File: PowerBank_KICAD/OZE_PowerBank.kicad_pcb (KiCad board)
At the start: 2 copper layers, 0 parts

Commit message: PCB layout
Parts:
- added 100k1: R, Resistor_SMD:R_0603_1608Metric_Pad0.98x0.95mm_HandSolder, F.Cu at (222.9, 121.0)
- added C1: 100nF, Capacitor_SMD:C_0805_2012Metric_Pad1.18x1.45mm_HandSolder, F.Cu at (129.5, 121.5)
- added C10: 22uF, Capacitor_SMD:C_0805_2012Metric_Pad1.18x1.45mm_HandSolder, F.Cu at (162.0, 84.0)
- added C11: 100n, Capacitor_SMD:C_0402_1005Metric, F.Cu at (186.6, 108.3)
- added C12: 10u, Capacitor_SMD:C_0805_2012Metric_Pad1.18x1.45mm_HandSolder, F.Cu at (176.5, 107.0)
- added C13: 100n, Capacitor_SMD:C_0402_1005Metric, F.Cu at (134.0, 83.0)
- added C14: 1u, Capacitor_SMD:C_0805_2012Metric_Pad1.18x1.45mm_HandSolder, F.Cu at (176.6, 109.5)
- added C15: 100n, Capacitor_SMD:C_0402_1005Metric, F.Cu at (178.6, 103.8)
- added C16: 1u, Capacitor_SMD:C_0805_2012Metric_Pad1.18x1.45mm_HandSolder, F.Cu at (176.6, 113.5)
- added C17: 1uF, Capacitor_SMD:C_0805_2012Metric_Pad1.18x1.45mm_HandSolder, F.Cu at (126.5, 54.0)
- added C18: 22uF, Capacitor_SMD:C_0805_2012Metric_Pad1.18x1.45mm_HandSolder, F.Cu at (126.5, 50.0)
- added C19: 1uF, Capacitor_SMD:C_0805_2012Metric_Pad1.18x1.45mm_HandSolder, F.Cu at (156.1, 57.0)
- added C2: 100nF, Capacitor_SMD:C_0805_2012Metric_Pad1.18x1.45mm_HandSolder, F.Cu at (130.7, 104.3)
- added C20: 1uF, Capacitor_SMD:C_0805_2012Metric_Pad1.18x1.45mm_HandSolder, F.Cu at (154.6, 61.5)
- added C21: 865060657011, 865060657011:CAPAE1030X1050N, F.Cu at (137.5, 48.8)
- added C22: 47uF, Capacitor_SMD:C_0805_2012Metric_Pad1.18x1.45mm_HandSolder, F.Cu at (213.2, 115.8)
- added C23: 47uF, Capacitor_SMD:C_0805_2012Metric_Pad1.18x1.45mm_HandSolder, F.Cu at (216.9, 116.0)
- added C24: 47uF, Capacitor_SMD:C_0805_2012Metric_Pad1.18x1.45mm_HandSolder, F.Cu at (209.7, 115.8)
- added C25: 10u, Capacitor_SMD:C_0805_2012Metric_Pad1.18x1.45mm_HandSolder, F.Cu at (210.1, 111.3)
- added C26: 0,1uF, Capacitor_SMD:C_0805_2012Metric_Pad1.18x1.45mm_HandSolder, F.Cu at (206.2, 115.8)
- added C27: 100n, Capacitor_SMD:C_0402_1005Metric, F.Cu at (214.1, 111.3)
- added C28: 865060657011, 865060657011:CAPAE1030X1050N, F.Cu at (196.4, 49.0)
- added C29: 22uF, Capacitor_SMD:C_0805_2012Metric_Pad1.18x1.45mm_HandSolder, F.Cu at (204.6, 44.5)
- added C3: 10p, Capacitor_SMD:C_0402_1005Metric, F.Cu at (176.5, 103.5)
- added C30: 100n, Capacitor_SMD:C_0402_1005Metric, F.Cu at (157.6, 66.0)
- added C31: 10uF, Capacitor_SMD:C_0805_2012Metric_Pad1.18x1.45mm_HandSolder, F.Cu at (220.6, 103.8)
- added C32: 10uF, Capacitor_SMD:C_0805_2012Metric_Pad1.18x1.45mm_HandSolder, F.Cu at (228.7, 114.8)
- added C33: 0,1uF, Capacitor_SMD:C_0805_2012Metric_Pad1.18x1.45mm_HandSolder, F.Cu at (205.1, 98.8)
- added C34: 22u, Capacitor_SMD:C_0805_2012Metric_Pad1.18x1.45mm_HandSolder, F.Cu at (166.0, 35.5)
- added C35: 22u, Capacitor_SMD:C_0805_2012Metric_Pad1.18x1.45mm_HandSolder, F.Cu at (216.3, 123.1)
- added C4: 4.7uF, Capacitor_SMD:C_0805_2012Metric_Pad1.18x1.45mm_HandSolder, F.Cu at (153.5, 84.4)
- added C5: 10u, Capacitor_SMD:C_0805_2012Metric_Pad1.18x1.45mm_HandSolder, F.Cu at (173.5, 84.5)
- added C6: 10p, Capacitor_SMD:C_0402_1005Metric, F.Cu at (176.5, 101.0)
- added C7: 100n, Capacitor_SMD:C_0402_1005Metric, F.Cu at (181.6, 95.8)
- added C8: 100n, Capacitor_SMD:C_0402_1005Metric, F.Cu at (191.6, 99.8)
- added C9: 100n, Capacitor_SMD:C_0402_1005Metric, F.Cu at (178.5, 99.7)
- added D1: BLUE, LED_SMD:LED_1206_3216Metric_Pad1.42x1.75mm_HandSolder, F.Cu at (195.6, 121.3)
- added D10: SMAJ5.0CA, Diode_SMD:D_SMA, F.Cu at (218.6, 97.8)
- added D2: RED, LED_SMD:LED_1206_3216Metric_Pad1.42x1.75mm_HandSolder, F.Cu at (167.5, 84.5)
- added D3: SD24_SOD323, Diode_SMD:D_SOD-323, F.Cu at (143.3, 74.7)
- added D4: SZMM3Z10VST1G, Diode_SMD:D_SOD-323, F.Cu at (143.4, 65.2)
- added D5: SS14, Diode_SMD:D_SMA, F.Cu at (177.6, 62.5)
- added D6: SS14, Diode_SMD:D_SMA, F.Cu at (152.1, 51.5)
- added D7: SS14, Diode_SMD:D_SMA, F.Cu at (165.6, 51.5)
- added D8: BLUE, LED_SMD:LED_1206_3216Metric_Pad1.42x1.75mm_HandSolder, F.Cu at (188.1, 66.0)
- added D9: SMAJ5.0CA, Diode_SMD:D_SMA, F.Cu at (213.6, 95.8)
- added F1: Polyfuse, Fuse:Fuse_2920_7451Metric_Pad2.10x5.45mm_HandSolder, F.Cu at (142.4, 83.0)
- added FB1: 120R, Resistor_SMD:R_0603_1608Metric_Pad0.98x0.95mm_HandSolder, F.Cu at (176.6, 111.5)
- added H1: MountingHole, MountingHole:MountingHole_2.2mm_M2_ISO7380, F.Cu at (233.5, 137.5)
- added H2: MountingHole, MountingHole:MountingHole_2.2mm_M2_ISO7380, F.Cu at (233.5, 33.0)
- added H3: MountingHole, MountingHole:MountingHole_2.2mm_M2_ISO7380, F.Cu at (123.0, 139.5)
- added H4: MountingHole, MountingHole:MountingHole_2.2mm_M2_ISO7380, F.Cu at (124.0, 31.5)
- added IC1: TPS25810RVCR, TPS25810RVCR:QFN50P300X400X80-21N, F.Cu at (222.4, 116.8)
- added IC2: TPS2514ADBVT, TPS2514ADBVT:SOT95P280X145-6N, F.Cu at (208.8, 98.8)
- added J1: Conn_01x02_Pin, TerminalBlock_Phoenix:TerminalBlock_Phoenix_PT-1,5-2-5.0-H_1x02_P5.00mm_Horizontal, F.Cu at (126.5, 79.5)
- added J10: USB_A, Connector_USB:USB_A_TE_292303-7_Horizontal, F.Cu at (230.6, 99.3)
- added J11: Conn_01x04_Pin, TerminalBlock_Phoenix:TerminalBlock_Phoenix_PT-1,5-4-3.5-H_1x04_P3.50mm_Horizontal, F.Cu at (159.2, 34.3)
- added J12: Conn_01x04_Pin, TerminalBlock_Phoenix:TerminalBlock_Phoenix_PT-1,5-4-5.0-H_1x04_P5.00mm_Horizontal, F.Cu at (209.0, 135.5)
- added J13: Conn_01x04_Pin, Connector_PinSocket_2.54mm:PinSocket_1x04_P2.54mm_Vertical, F.Cu at (169.2, 79.4)
- added J14: Conn_01x04_Pin, Connector_PinSocket_2.54mm:PinSocket_1x04_P2.54mm_Vertical, F.Cu at (217.7, 127.5)
- added J15: Conn_01x04_Pin, Connector_PinSocket_2.54mm:PinSocket_1x04_P2.54mm_Vertical, F.Cu at (180.1, 35.5)
- added J16: Conn_01x02_Pin, Connector_JST:JST_XH_B2B-XH-A_1x02_P2.50mm_Vertical, F.Cu at (229.0, 44.0)
- added J17: Battery with BMS Input, TerminalBlock_Phoenix:TerminalBlock_Phoenix_PT-1,5-2-5.0-H_1x02_P5.00mm_Horizontal, F.Cu at (226.9, 61.0)
- added J2: DCJ200-10-A-XX-K_REVA, Connector_BarrelJack:BarrelJack_GCT_DCJ200-10-A_Horizontal, F.Cu at (130.3, 67.5)
- added J3: Conn_01x04_Pin, Connector_PinSocket_2.54mm:PinSocket_1x04_P2.54mm_Vertical, F.Cu at (194.6, 79.3)
- added J4: Conn_01x04_Pin, Connector_PinSocket_2.54mm:PinSocket_1x04_P2.54mm_Vertical, F.Cu at (182.8, 121.2)
- added J5: Conn_01x04_Pin, Connector_PinSocket_2.54mm:PinSocket_1x04_P2.54mm_Vertical, F.Cu at (187.6, 79.3)
- added J6: Conn_01x04_Pin, Connector_PinSocket_2.54mm:PinSocket_1x04_P2.54mm_Vertical, F.Cu at (201.1, 79.3)
- added J7: Conn_01x10_Pin, Connector_PinSocket_2.54mm:PinSocket_1x10_P2.54mm_Vertical, F.Cu at (211.1, 65.1)
- added J8: Conn_01x10_Pin, Connector_PinSocket_2.54mm:PinSocket_1x10_P2.54mm_Vertical, F.Cu at (158.5, 105.5)
- added J9: USB_C_Receptacle_PowerOnly_6P, Connector_USB:USB_C_Receptacle_GCT_USB4125-xx-x-0190_6P_TopMnt_Horizontal, F.Cu at (234.7, 117.8)
- added L1: 150uH, Inductor_SMD:L_Pulse_PA4320, F.Cu at (181.1, 48.5)
- added Q1: IRLML6402TRPBF, IRLML6402TRPBF:SOT95P237X112-3N, F.Cu at (143.4, 70.1)
- added Q2: IRLZ44N, Package_TO_SOT_THT:TO-220-3_Vertical, F.Cu at (148.0, 45.5)
- added Q3: IRLZ44N, Package_TO_SOT_THT:TO-220-3_Vertical, F.Cu at (161.6, 45.5)
- added R1: 10k, Resistor_SMD:R_0805_2012Metric_Pad1.20x1.40mm_HandSolder, F.Cu at (126.5, 121.5)
- added R10: 0, Resistor_SMD:R_0805_2012Metric_Pad1.20x1.40mm_HandSolder, F.Cu at (164.0, 115.6)
- added R11: 0, Resistor_SMD:R_0805_2012Metric_Pad1.20x1.40mm_HandSolder, F.Cu at (164.0, 119.1)
- added R12: 10k, Resistor_SMD:R_0805_2012Metric_Pad1.20x1.40mm_HandSolder, F.Cu at (147.9, 65.7)
- added R13: 9k1, Resistor_SMD:R_0805_2012Metric_Pad1.20x1.40mm_HandSolder, F.Cu at (124.5, 44.5)
- added R14: 1k, Resistor_SMD:R_0805_2012Metric_Pad1.20x1.40mm_HandSolder, F.Cu at (129.0, 44.5)
- added R15: 100k, Resistor_SMD:R_0402_1005Metric, F.Cu at (162.1, 66.0)
- added R16: 20k, Resistor_SMD:R_0805_2012Metric_Pad1.20x1.40mm_HandSolder, F.Cu at (164.6, 64.0)
- added R17: 22, Resistor_SMD:R_0805_2012Metric_Pad1.20x1.40mm_HandSolder, F.Cu at (148.1, 51.0)
- added R18: 22, Resistor_SMD:R_0805_2012Metric_Pad1.20x1.40mm_HandSolder, F.Cu at (161.1, 51.0)
- added R19: 100k, Resistor_SMD:R_0402_1005Metric, F.Cu at (225.5, 112.1)
- added R2: 1k5, Resistor_SMD:R_0805_2012Metric_Pad1.20x1.40mm_HandSolder, F.Cu at (185.1, 117.3)
- added R20: 100k, Resistor_SMD:R_0402_1005Metric, F.Cu at (222.5, 112.0)
- added R21: 100k, Resistor_SMD:R_0402_1005Metric, F.Cu at (219.0, 112.0)
- added R22: 1k, Resistor_SMD:R_0805_2012Metric_Pad1.20x1.40mm_HandSolder, F.Cu at (188.1, 60.0)
- added R23: 50m, Resistor_SMD:R_1206_3216Metric_Pad1.30x1.75mm_HandSolder, F.Cu at (211.1, 43.5)
- added R24: 27k, Resistor_SMD:R_0805_2012Metric_Pad1.20x1.40mm_HandSolder, F.Cu at (217.0, 44.0)
- added R25: 10k, Resistor_SMD:R_0805_2012Metric_Pad1.20x1.40mm_HandSolder, F.Cu at (217.0, 49.0)
- added R3: 47, Resistor_SMD:R_0805_2012Metric_Pad1.20x1.40mm_HandSolder, F.Cu at (195.6, 114.8)
- added R4: 1k5, Resistor_SMD:R_0805_2012Metric_Pad1.20x1.40mm_HandSolder, F.Cu at (189.1, 117.3)
- added R5: 10k, Resistor_SMD:R_0805_2012Metric_Pad1.20x1.40mm_HandSolder, F.Cu at (127.7, 104.3)
- added R6: 100R, Resistor_SMD:R_0805_2012Metric_Pad1.20x1.40mm_HandSolder, F.Cu at (167.5, 89.5)
- added R7: 0, Resistor_SMD:R_0805_2012Metric_Pad1.20x1.40mm_HandSolder, F.Cu at (164.0, 105.0)
- added R8: 0, Resistor_SMD:R_0805_2012Metric_Pad1.20x1.40mm_HandSolder, F.Cu at (164.0, 108.6)
- added R9: 0, Resistor_SMD:R_0805_2012Metric_Pad1.20x1.40mm_HandSolder, F.Cu at (164.0, 112.0)
- added SW1: SW_Push, Button_Switch_THT:SW_PUSH-12mm_Wuerth-430476085716, F.Cu at (146.5, 125.5)
- added SW2: SW_SPDT, LIB_SLW-1276864-4A-D:SLW12768644AD, F.Cu at (135.8, 105.5)
- added U1: TLV70233_SOT23-5, Package_TO_SOT_SMD:SOT-23-5, F.Cu at (157.8, 84.0)
- added U2: STM32F103C8Tx, Package_QFP:LQFP-48_7x7mm_P0.5mm, F.Cu at (184.7, 102.0)
- added U3: LM5106SD, Package_SON:WSON-10-1EP_4x4mm_P0.8mm_EP2.6x3mm_ThermalVias, F.Cu at (159.2, 61.2)
- added U4: INA180A1, Package_TO_SOT_SMD:SOT-23-5, F.Cu at (210.9, 48.5)
- added Y1: 16MHz, LFXTAL071744Reel:LFXTAL071744Reel, F.Cu at (172.6, 102.3)
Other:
- board outline added: 118 x 114.8 mm
- copper layers 2 -> 4

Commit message: before branching
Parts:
- moved D3 1.15 mm to (144.5, 74.7)
- moved R12 0.57 mm to (148.5, 65.5)
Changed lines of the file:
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@@
 	(footprint "Resistor_SMD:R_0805_2012Metric_Pad1.20x1.40mm_HandSolder"
 		(layer "F.Cu")
-		(at 147.95 65.65)
+		(at 148.5 65.5)
 		(descr "Resistor SMD 0805 (2012 Metric), square (rectangular) end terminal, IPC-7351 nominal with elongated pad for handsoldering. (Body size source: IPC-SM-782 page 72, https://www.pcb-3d.com/wordpress/wp-content/uploads/ipc-sm-782a_amendment_1_and_2.pdf), generated with kicad-footprint-generator")
 		(tags "resistor handsolder")
@@
 	(footprint "Diode_SMD:D_SOD-323"
 		(layer "F.Cu")
-		(at 143.35 74.65 180)
+		(at 144.5 74.65 180)
 		(descr "SOD-323")
 		(tags "SOD-323")

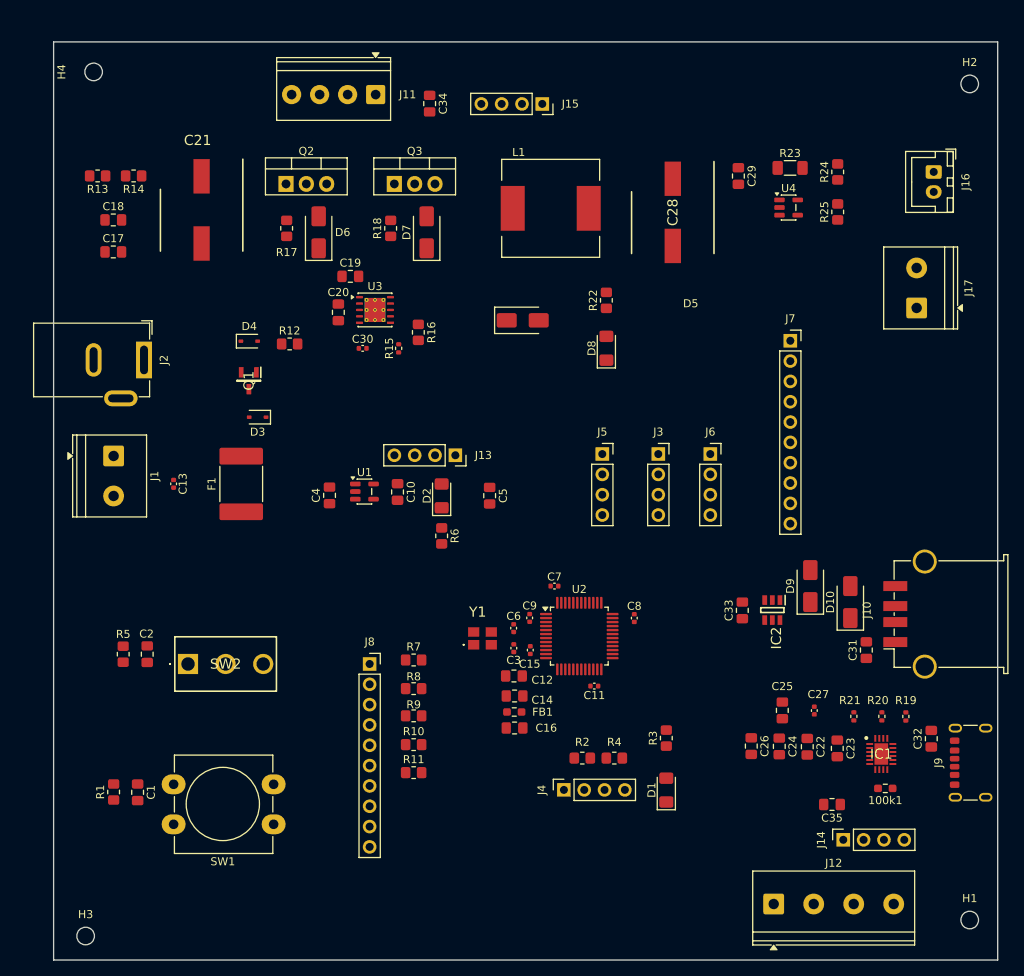
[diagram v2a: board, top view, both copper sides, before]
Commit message: 26.11 Hubert - PCB
Poprowadzone ścieżki sygnałowe, prądowe, poza 2 wchodzącymi do sterownika USB-C, USB-A . Brak wylanej masy
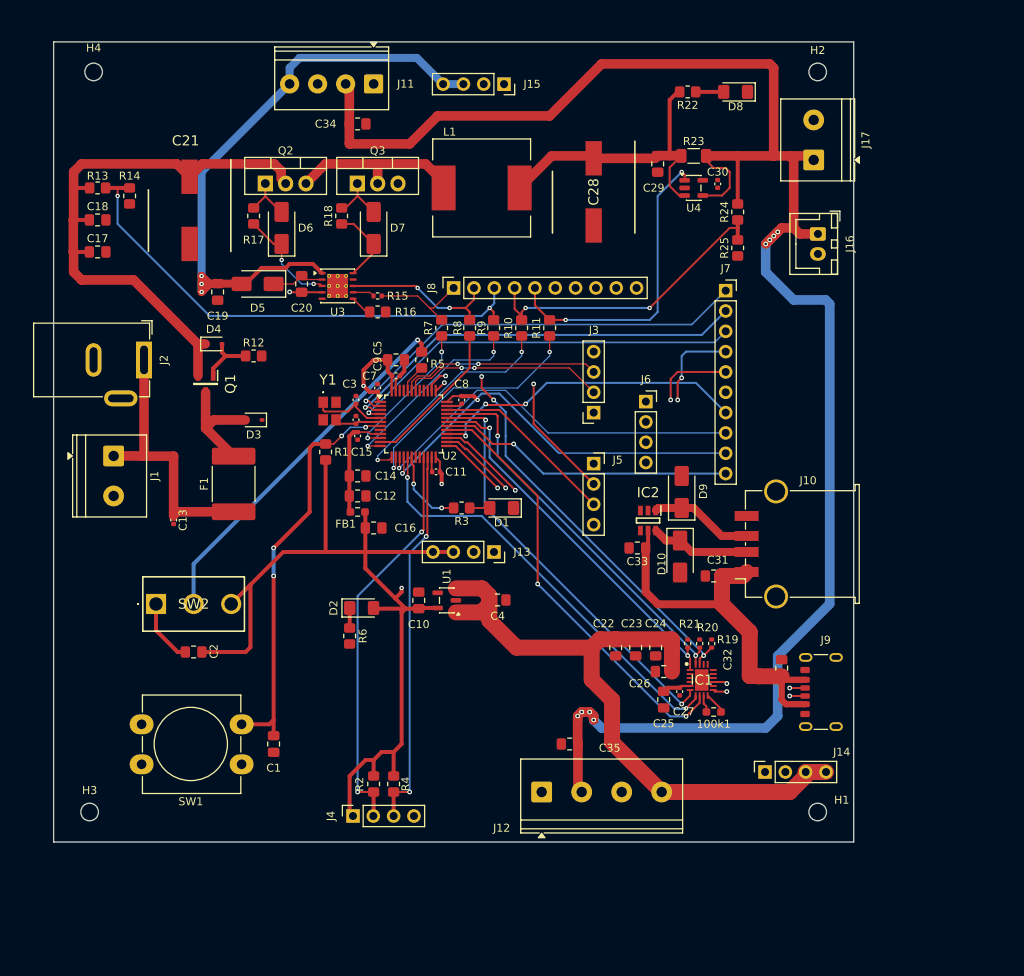
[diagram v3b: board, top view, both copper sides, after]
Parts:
- moved R11 58.1 mm to (181.0, 63.5), turned to 90 degrees
- moved R10 53.8 mm to (177.5, 63.5), turned to 90 degrees
- moved R5 52.4 mm to (165.0, 67.5), turned to -90 degrees
- moved R1 50.1 mm to (153.0, 79.0), turned to -90 degrees
- moved R9 49.5 mm to (174.0, 63.5), turned to 90 degrees
- moved C30 48.9 mm to (202.0, 45.5), turned to -90 degrees
- moved J8 48.2 mm to (169.0, 58.5), turned to 90 degrees
- moved R8 45.6 mm to (171.0, 63.5), turned to 90 degrees
- moved R7 41.6 mm to (167.5, 63.5), turned to 90 degrees
- moved D1 40.8 mm to (175.0, 86.0), turned to 180 degrees
- moved R3 38.5 mm to (170.0, 86.0), turned to 180 degrees
- moved C3 36.8 mm to (156.8, 72.5), turned to 90 degrees
- moved D8 35.9 mm to (204.2, 34.0), turned to 180 degrees
- moved C8 34.8 mm to (170.0, 72.5)
- moved C9 34.6 mm to (161.8, 69.5), turned to 0 degrees
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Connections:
- net Net-(C28-+) renamed /V_in_po_L1
- net Net-(D5-K) renamed /HB
- net Net-(D6-A) renamed /Q2_bramka
- net Net-(D6-K) renamed /HO
- net Net-(D7-A) renamed /Q3_bramka
- net Net-(D7-K) renamed /LO
- net Net-(D8-A) renamed /V_led_blue
- net Net-(U2-PA0) renamed /ENABLE_STM
- net Net-(U2-PA1) renamed /PWM_STM
- net Net-(U2-PA2) renamed /V_BEFOREBUCK_STM
- net Net-(U2-PA3) renamed /V_BAT_STM
- net Net-(U2-PA4) renamed /I_OUT_STM
- net Net-(U3-EN) renamed /ENABLE_IN
- C12 pad 1: Net-(C12-Pad1) -> Net-(U2-VDDA)
- C14 pad 1: Net-(C12-Pad1) -> Net-(U2-VDDA)
- C15 pad 1: Net-(C12-Pad1) -> Net-(U2-VDDA)
- C22 pad 1: unconnected-(C22-Pad1) -> +5V
- C33 pad 2: unconnected-(C33-Pad2) -> GND
- FB1 pad 1: Net-(C12-Pad1) -> Net-(U2-VDDA)
- U2 pad 9: GND -> Net-(U2-VDDA)
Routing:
- net +3.3V: track 0.00 -> 234.7 mm, vias 0 -> 4
- net P+: track 0.00 -> 231.9 mm, vias 0 -> 8
- net +5V: track 0.00 -> 84.5 mm
- net +12V: track 0.00 -> 77.6 mm, vias 0 -> 3
- net VIN: track 0.00 -> 71.8 mm
- net V_beforeBUCK: track 0.00 -> 63.7 mm, vias 0 -> 2
- net PB12: track 0.00 -> 62.0 mm, vias 0 -> 3
- net PB13: track 0.00 -> 59.2 mm, vias 0 -> 2
- net UFP: track 0.00 -> 56.6 mm, vias 0 -> 4
- net PB14: track 0.00 -> 56.3 mm, vias 0 -> 1
- net CHG_HI: track 0.00 -> 54.5 mm, vias 0 -> 2
- net CHG: track 0.00 -> 53.6 mm, vias 0 -> 2
- net ENABLE_TPS: track 0.00 -> 52.9 mm, vias 0 -> 2
- net PC13: track 0.00 -> 52.7 mm, vias 0 -> 1
- net PC14: track 0.00 -> 52.0 mm, vias 0 -> 1
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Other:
- board size 118 x 114.8 mm -> 100 x 100 mm

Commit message: Płytka PCB i ścieżki w zasadzie skończone 'prawie'
Wylane warstwy, wszystkie połączenia poza dwoma od przycisku z których nie korzystamy, jeszcze są błędy jakieś związane z termal padami, ale juz możesz wprowadzać zmiany
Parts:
- moved D10 0.60 mm to (197.5, 91.5)
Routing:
- net +3.3V: track 234.7 -> 324.2 mm, vias 4 -> 7
- net GND: track 16.2 -> 52.5 mm, vias 0 -> 678
- net CHG: track 53.6 -> 86.5 mm, vias 2 -> 3
- net CHG_HI: track 54.5 -> 84.6 mm, vias 2 -> 3
- net /VBUS: track 48.8 -> 51.6 mm
- net /D+: track 12.9 -> 15.0 mm
- net P+: track 231.9 -> 233.6 mm
- net +5V: track 84.5 -> 85.9 mm
- net PA5: track 48.4 -> 47.1 mm
- net /V_in_po_L1: track 37.5 -> 38.6 mm
- net UFP: track 56.6 -> 57.5 mm
- net /D-: track 12.4 -> 13.2 mm
- net PC14: track 52.0 -> 52.8 mm
- net PA6: track 49.8 -> 50.4 mm
- net /SW_BOOT0: track 46.3 -> 46.9 mm
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- added copper zone on F.Cu, net +5V
- added copper zone on F.Cu, net /VBUS
- added copper zone on B.Cu, net GND
- added copper zone on F.Cu, net GND
- added copper zone on In1.Cu, net GND
- added copper zone on In2.Cu, net GND

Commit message: changed footprint, correct GND conection to thermal, remove some vias, give additional vias in TPS25810
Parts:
- C1, C12, C14, C16, C17, C19, C2, C25, C26, C31, C32, C33: footprint Capacitor_SMD:C_0805_2012Metric_Pad1.18x1.45mm_HandSolder -> PCM_JLCPCB:C_0805
- C11, C15, C27, C3, C30, C6, C7, C8, C9: footprint Capacitor_SMD:C_0402_1005Metric -> PCM_JLCPCB:C_0402
- C13: footprint Capacitor_SMD:C_0402_1005Metric -> Capacitor_SMD:C_0805_2012Metric
- R10, R11, R7, R8, R9: footprint Resistor_SMD:R_0805_2012Metric_Pad1.20x1.40mm_HandSolder -> PCM_JLCPCB:R_0805
- moved C7 0.16 mm to (159.5, 70.8)
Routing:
- net GND: track 52.5 -> 51.8 mm, vias 678 -> 464
- net I_OUT: track 38.6 -> 39.2 mm
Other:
- board text added: "12V"
- board text added: "3.3V"
- board text added: "5V"
- board text added: "BMS"
- board text added: "C"
- board text added: "C_HI"
- board text added: "EN"
- board text added: "FLASH"
- board text added: "GND"
- board text added: "I_OUT"
- board text added: "NC"
- board text added: "P+"
- board text added: "PA5"
- board text added: "PA6"
- board text added: "PA9"
- board text added: "PB12"
- board text added: "PB13"
- board text added: "PB14"
- board text added: "PB15"
- board text added: "PC13"
- board text added: "PC14"
- board text added: "PC15"
- board text added: "PV"
- board text added: "PWM"
- board text added: "Przetwornica 12V"
- board text added: "Przetwornica 5V"
- board text added: "RESET"
- board text added: "RUN"
- board text added: "SWCLK"
- board text added: "SWDIO"
- board text added: "V_BAT"
- board text added: "V_BB"
